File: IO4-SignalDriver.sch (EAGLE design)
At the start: 24 parts, among them CON2 CONNECTOR-GROVE-4P-2.0-347013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, CON3 CONNECTOR-GROVE-4P-2.0-347013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, IC1 74LS139D, P1 500R, P2 500R, P3 500R, P4 500R, P5 500R, P6 500R

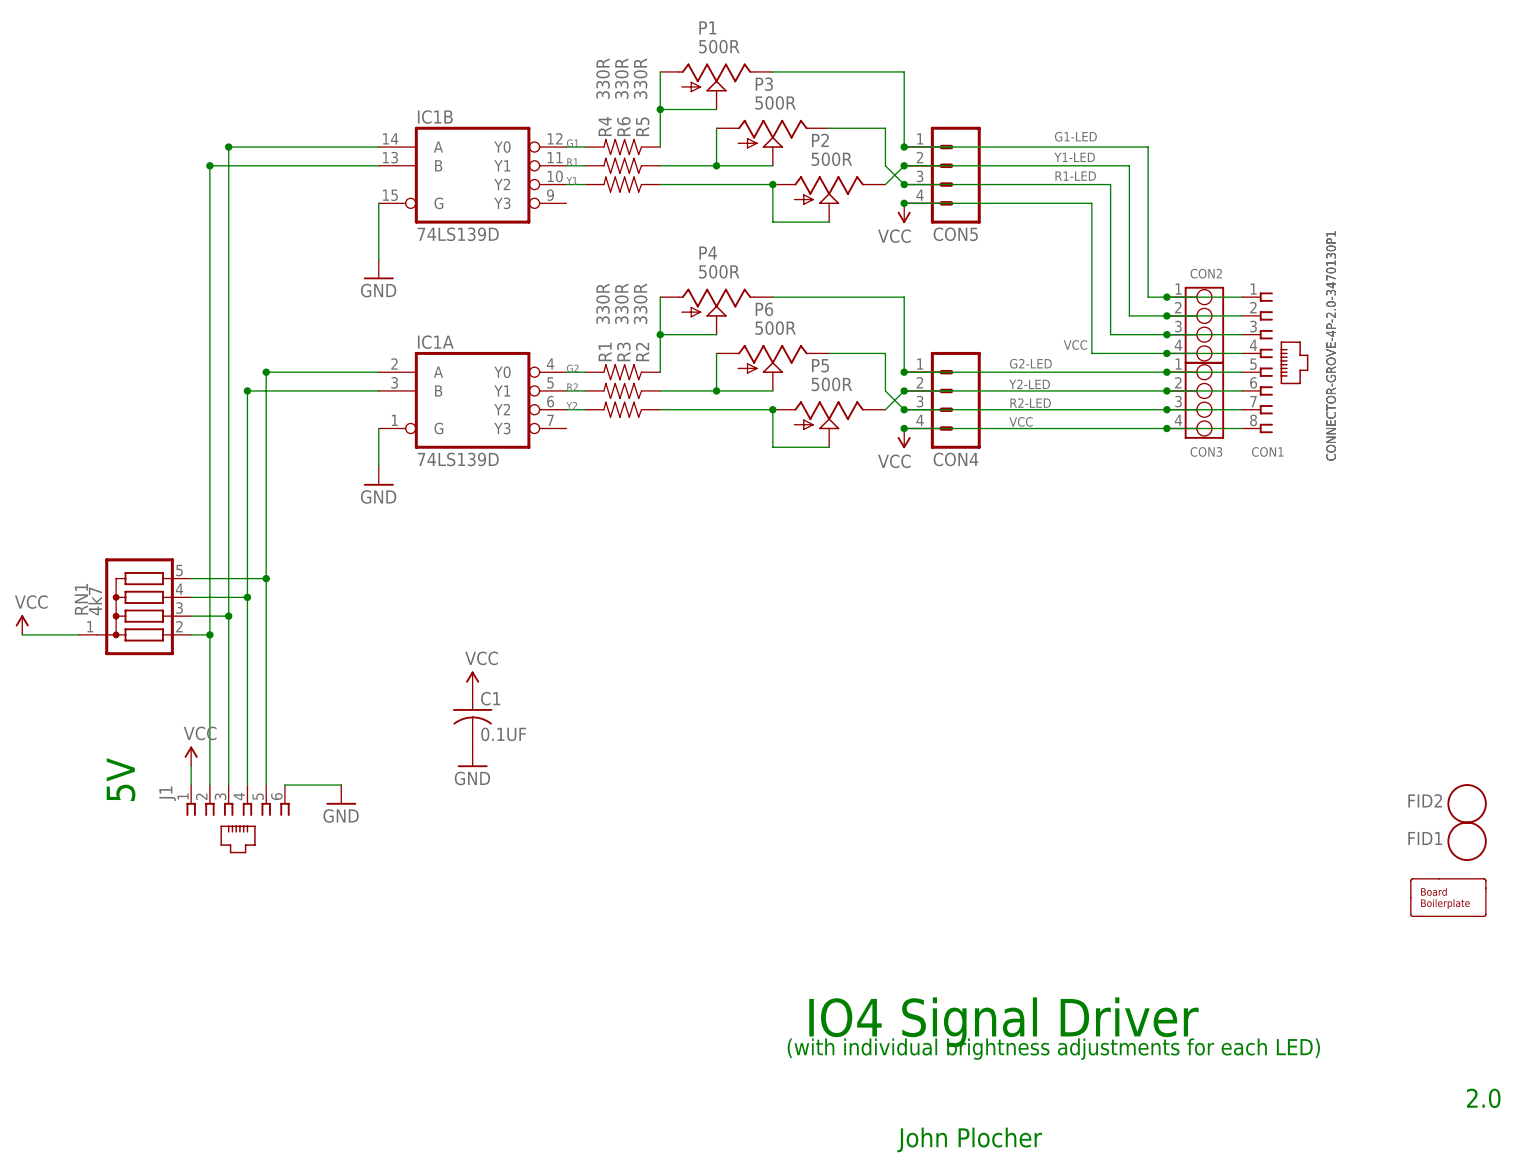
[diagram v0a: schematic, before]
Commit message: FID placement & SPCoast update
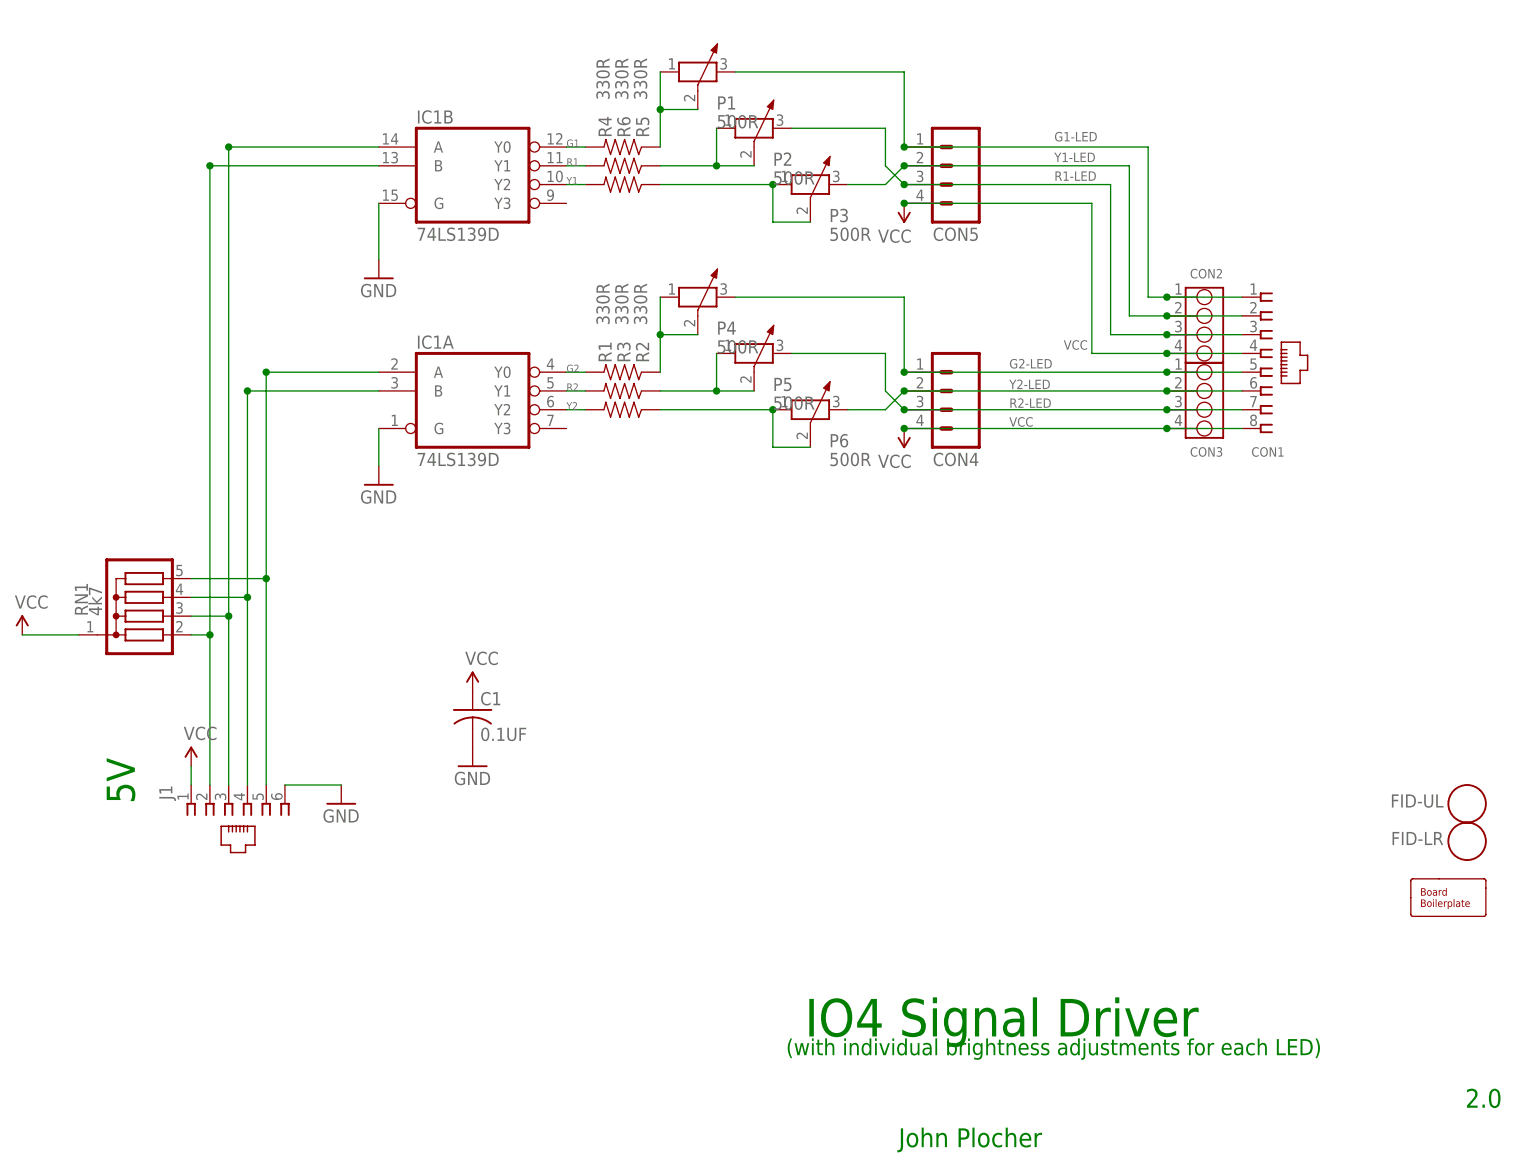
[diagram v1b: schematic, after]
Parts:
- CON2, CON3: value CONNECTOR-GROVE-4P-2.0-3470130P1 -> (none)
- P1, P2, P3, P4, P5, P6: device SPCoast:TRIM_US-W-1 -> SPCoast:R-POTENTIOMETERP-3319
- renumbered FID1 to FID-LR, FID2 to FID-UL
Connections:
- net G1-LED: now also P1.3; no longer P1.CW
- net G1V: now also P1.1, P1.2; no longer P1.CCW, P1.W
- net G2-LED: now also P4.3; no longer P4.CW
- net G2V: now also P4.1, P4.2; no longer P4.CCW, P4.W
- net R1-LED: now also P2.3; no longer P3.CW
- net R1V: now also P2.1, P2.2; no longer P3.CCW, P3.W
- net R2-LED: now also P5.3; no longer P6.CW
- net R2V: now also P5.1, P5.2; no longer P6.CCW, P6.W
- net Y1-LED: now also P3.3; no longer P2.CW
- net Y1V: now also P3.1, P3.2; no longer P2.CCW, P2.W
- net Y2-LED: now also P6.3; no longer P5.CW
- net Y2V: now also P6.1, P6.2; no longer P5.CCW, P5.W

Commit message: added values for connectors
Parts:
- CON1: value (none) -> RJ45
- CON2, CON3: value (none) -> 2mm
- CON4, CON5: value (none) -> 3.5mm
- J1: value (none) -> RJ12/6
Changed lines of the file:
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@@
 <part name="R6" library="SPCoast" deviceset="R*" device="0805-RES" value="330R"/>
 <part name="R4" library="SPCoast" deviceset="R*" device="0805-RES" value="330R"/>
-<part name="CON4" library="SparkFun" deviceset="M04" device="SCREW_LOCK"/>
-<part name="CON5" library="SparkFun" deviceset="M04" device="SCREW_LOCK"/>
+<part name="CON4" library="SparkFun" deviceset="M04" device="SCREW_LOCK" value="3.5mm"/>
+<part name="CON5" library="SparkFun" deviceset="M04" device="SCREW_LOCK" value="3.5mm"/>
 <part name="RN1" library="resistor-sil" deviceset="G04R" device="" value="4k7"/>
-<part name="J1" library="SPCoast" deviceset="CONNECTOR-RJ25" device="-6P6C"/>
+<part name="J1" library="SPCoast" deviceset="CONNECTOR-RJ25" device="-6P6C" value="RJ12/6"/>
 <part name="P+5" library="SparkFun" deviceset="VCC" device=""/>
 <part name="GND4" library="SparkFun" deviceset="GND" device=""/>
-<part name="CON1" library="SPCoast" deviceset="CONNECTOR-RJ45" device="-FRONT"/>
+<part name="CON1" library="SPCoast" deviceset="CONNECTOR-RJ45" device="-FRONT" value="RJ45"/>
 <part name="BOARD1" library="SPCoast" deviceset="BOARD" device="80X100"/>
 <part name="P+6" library="SparkFun" deviceset="VCC" device=""/>
 <part name="P+7" library="SparkFun" deviceset="VCC" device=""/>
-<part name="CON2" library="SPCoast" deviceset="CONNECTOR-GROVE-4P-2.0" device="-3470130P1"/>
-<part name="CON3" library="SPCoast" deviceset="CONNECTOR-GROVE-4P-2.0" device="-3470130P1"/>
+<part name="CON2" library="SPCoast" deviceset="CONNECTOR-GROVE-4P-2.0" device="-3470130P1" value="2mm"/>
+<part name="CON3" library="SPCoast" deviceset="CONNECTOR-GROVE-4P-2.0" device="-3470130P1" value="2mm"/>
 <part name="FID-LR" library="SPCoast" deviceset="FIDUCIAL" device=""/>
 <part name="FID-UL" library="SPCoast" deviceset="FIDUCIAL" device=""/>

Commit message: normalized values
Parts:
- BOARD1: value BOARD80X100 -> BOARD
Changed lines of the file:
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@@
 <part name="GND4" library="SparkFun" deviceset="GND" device=""/>
 <part name="CON1" library="SPCoast" deviceset="CONNECTOR-RJ45" device="-FRONT" value="RJ45"/>
-<part name="BOARD1" library="SPCoast" deviceset="BOARD" device="80X100"/>
+<part name="BOARD1" library="SPCoast" deviceset="BOARD" device="80X100" value="BOARD"/>
 <part name="P+6" library="SparkFun" deviceset="VCC" device=""/>
 <part name="P+7" library="SparkFun" deviceset="VCC" device=""/>
